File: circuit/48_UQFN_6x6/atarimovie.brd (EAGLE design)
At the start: 72.4 x 82.5 mm, 24 parts, among them IC1 AMS1117-3.3V, J1 CARTRIDGE EDGE, J2 TF-15X15, U1 DSPIC33CKXXMC105-X_M4, U2 74LVCH245APW,118, U3 74LVCH245APW,118, X1 22-23-2051

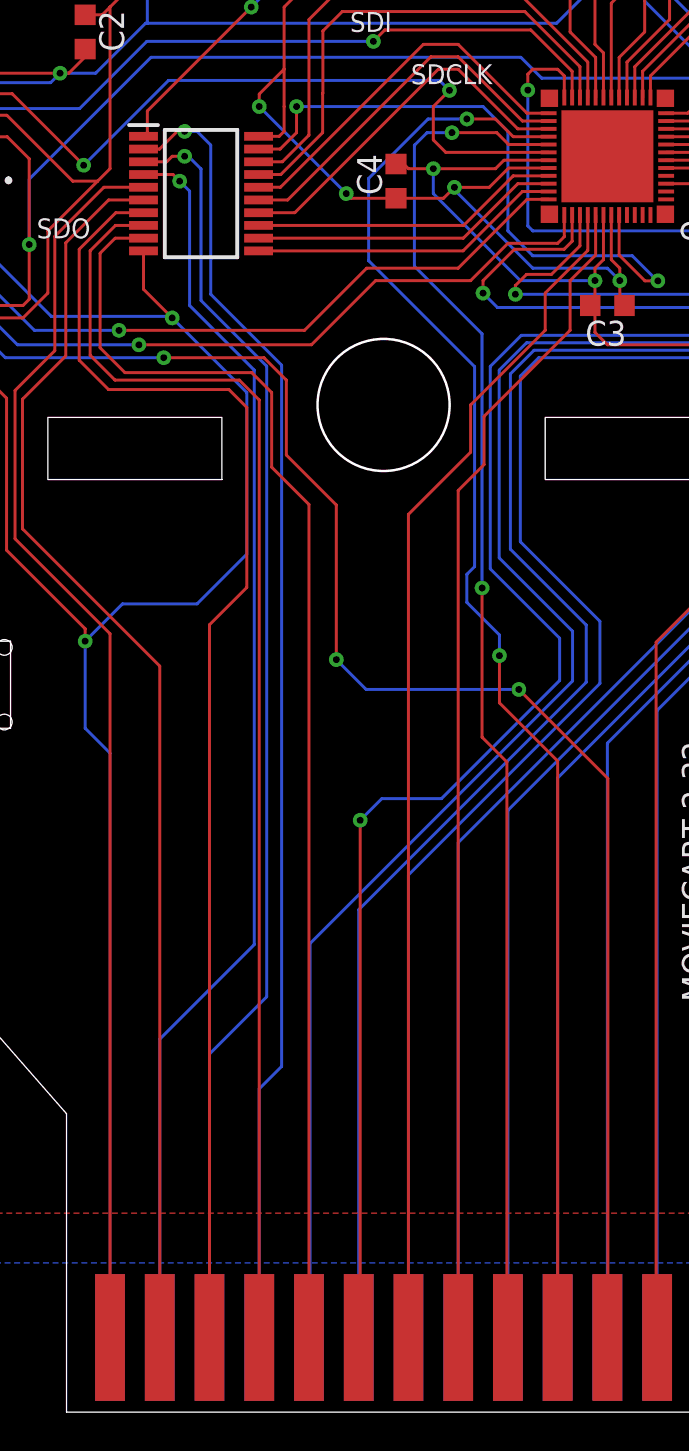
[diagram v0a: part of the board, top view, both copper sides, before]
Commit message: gerber files and rerouting away from post hole slightly
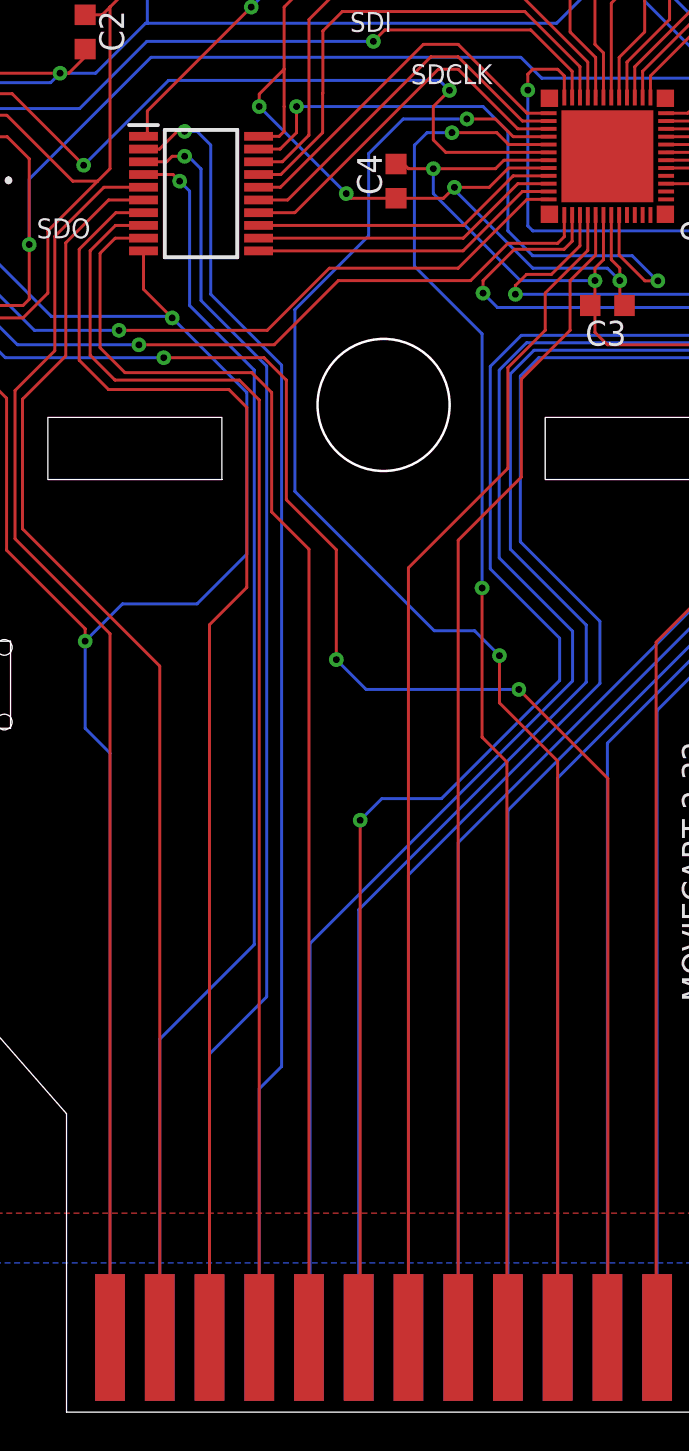
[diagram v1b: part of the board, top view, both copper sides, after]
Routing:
- net CADDR8: track 74.3 -> 79.1 mm
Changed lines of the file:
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@@
 <wire x1="42.7482" y1="38.6334" x2="42.7482" y2="36.2204" width="0.1524" layer="1"/>
 <wire x1="45.72" y1="3.81" x2="45.72" y2="33.2486" width="0.1524" layer="1"/>
-<wire x1="41.0845" y1="66.04" x2="39.1033" y2="66.04" width="0.1524" layer="16"/>
+<wire x1="41.0845" y1="66.04" x2="37.8333" y2="66.04" width="0.1524" layer="16"/>
 <via x="42.7482" y="38.6334" extent="1-16" drill="0.35"/>
-<wire x1="36.068" y1="58.801" x2="36.068" y2="63.0047" width="0.1524" layer="16"/>
-<wire x1="39.1033" y1="66.04" x2="36.068" y2="63.0047" width="0.1524" layer="16"/>
-<wire x1="41.4782" y1="53.3908" x2="41.4782" y2="43.18" width="0.1524" layer="16"/>
-<wire x1="41.4782" y1="53.3908" x2="36.068" y2="58.801" width="0.1524" layer="16"/>
-<wire x1="42.7482" y1="39.6875" x2="42.7482" y2="38.6334" width="0.1524" layer="16"/>
-<wire x1="41.4782" y1="43.18" x2="41.0845" y2="42.7863" width="0.1524" layer="16"/>
-<wire x1="41.0845" y1="42.7863" x2="41.0845" y2="41.3512" width="0.1524" layer="16"/>
-<wire x1="41.0845" y1="41.3512" x2="42.7482" y2="39.6875" width="0.1524" layer="16"/>
+<wire x1="36.068" y1="60.071" x2="36.068" y2="64.2747" width="0.1524" layer="16"/>
+<wire x1="37.8333" y1="66.04" x2="36.068" y2="64.2747" width="0.1524" layer="16"/>
+<wire x1="41.4782" y1="39.9034" x2="42.7482" y2="38.6334" width="0.1524" layer="16"/>
+<wire x1="41.4782" y1="39.9034" x2="39.41705" y2="39.9034" width="0.1524" layer="16"/>
+<wire x1="39.41705" y1="39.9034" x2="32.3013" y2="47.01915" width="0.1524" layer="16"/>
+<wire x1="32.3013" y1="56.3043" x2="36.068" y2="60.071" width="0.1524" layer="16"/>
+<wire x1="32.3013" y1="47.01915" x2="32.3013" y2="56.3043" width="0.1524" layer="16"/>
 </signal>
 <signal name="CADDR9">
@@
 <wire x1="47.26" y1="59.325" x2="45.085" y2="57.15" width="0.1524" layer="1"/>
 <wire x1="45.085" y1="57.15" x2="45.085" y2="55.245" width="0.1524" layer="1"/>
-<wire x1="38.1" y1="3.81" x2="38.1" y2="45.847" width="0.1524" layer="1"/>
-<wire x1="38.1" y1="45.847" x2="41.275" y2="49.022" width="0.1524" layer="1"/>
-<wire x1="41.275" y1="49.022" x2="41.275" y2="51.435" width="0.1524" layer="1"/>
-<wire x1="45.085" y1="55.245" x2="41.275" y2="51.435" width="0.1524" layer="1"/>
+<wire x1="38.1" y1="3.81" x2="38.1" y2="43.1165" width="0.1524" layer="1"/>
+<wire x1="38.1" y1="43.1165" x2="43.18" y2="48.1965" width="0.1524" layer="1"/>
+<wire x1="43.18" y1="48.1965" x2="43.18" y2="53.34" width="0.1524" layer="1"/>
+<wire x1="45.085" y1="55.245" x2="43.18" y2="53.34" width="0.1524" layer="1"/>
 </signal>
 <signal name="CADDR12">
@@
 <wire x1="45.259996875" y1="61.935" x2="44.155" y2="61.935" width="0.1524" layer="1"/>
 <wire x1="44.155" y1="61.935" x2="40.64" y2="58.42" width="0.1524" layer="1"/>
-<wire x1="32.7914" y1="55.245" x2="23.3172" y2="55.245" width="0.1524" layer="1"/>
-<wire x1="35.9664" y1="58.42" x2="32.7914" y2="55.245" width="0.1524" layer="1"/>
-<wire x1="40.64" y1="58.42" x2="35.9664" y2="58.42" width="0.1524" layer="1"/>
+<wire x1="30.8864" y1="55.245" x2="23.3172" y2="55.245" width="0.1524" layer="1"/>
+<wire x1="34.0614" y1="58.42" x2="30.8864" y2="55.245" width="0.1524" layer="1"/>
+<wire x1="40.64" y1="58.42" x2="34.0614" y2="58.42" width="0.1524" layer="1"/>
 <via x="23.3172" y="55.245" extent="1-16" drill="0.35"/>
 <wire x1="23.3172" y1="55.245" x2="18.9992" y2="55.245" width="0.1524" layer="16"/>
@@
 <contactref element="U1" pad="37"/>
 <wire x1="46.06" y1="60.03" x2="46.06" y2="61.134996875" width="0.1524" layer="1"/>
-<wire x1="24.3332" y1="54.5084" x2="33.147" y2="54.5084" width="0.1524" layer="1"/>
+<wire x1="24.3332" y1="54.5084" x2="31.242" y2="54.5084" width="0.1524" layer="1"/>
 <via x="24.3332" y="54.5084" extent="1-16" drill="0.35"/>
-<wire x1="36.4236" y1="57.785" x2="41.275" y2="57.785" width="0.1524" layer="1"/>
+<wire x1="34.5186" y1="57.785" x2="41.275" y2="57.785" width="0.1524" layer="1"/>
 <wire x1="45.72" y1="59.69" x2="46.06" y2="60.03" width="0.1524" layer="1"/>
-<wire x1="33.147" y1="54.5084" x2="36.4236" y2="57.785" width="0.1524" layer="1"/>
+<wire x1="31.242" y1="54.5084" x2="34.5186" y2="57.785" width="0.1524" layer="1"/>
 <wire x1="5.08" y1="78.74" x2="3.7465" y2="77.4065" width="0.1524" layer="16"/>
 <wire x1="3.7465" y1="68.8975" x2="3.7465" y2="77.4065" width="0.1524" layer="16"/>
@@
 <wire x1="47.66" y1="59.09" x2="46.355" y2="57.785" width="0.1524" layer="1"/>
 <wire x1="46.355" y1="57.785" x2="46.355" y2="55.245" width="0.1524" layer="1"/>
-<wire x1="40.64" y1="47.06694375" x2="40.64" y2="3.81" width="0.1524" layer="1"/>
-<wire x1="41.9608" y1="50.8508" x2="41.9608" y2="48.38774375" width="0.1524" layer="1"/>
-<wire x1="46.355" y1="55.245" x2="41.9608" y2="50.8508" width="0.1524" layer="1"/>
-<wire x1="41.9608" y1="48.38774375" x2="40.64" y2="47.06694375" width="0.1524" layer="1"/>
+<wire x1="40.64" y1="44.52694375" x2="40.64" y2="3.81" width="0.1524" layer="1"/>
+<wire x1="43.8658" y1="52.7558" x2="43.8658" y2="47.75274375" width="0.1524" layer="1"/>
+<wire x1="46.355" y1="55.245" x2="43.8658" y2="52.7558" width="0.1524" layer="1"/>
+<wire x1="43.8658" y1="47.75274375" x2="40.64" y2="44.52694375" width="0.1524" layer="1"/>
 </signal>
 <signal name="CDATA0">
@@
 <wire x1="23.622" y1="53.086" x2="30.099" y2="53.086" width="0.1524" layer="1"/>
 <wire x1="30.099" y1="53.086" x2="31.115" y2="52.07" width="0.1524" layer="1"/>
-<wire x1="31.115" y1="48.26" x2="33.02" y2="46.355" width="0.1524" layer="1"/>
-<wire x1="31.115" y1="52.07" x2="31.115" y2="48.26" width="0.1524" layer="1"/>
-<wire x1="33.02" y1="46.355" x2="33.02" y2="3.81" width="0.1524" layer="1"/>
+<wire x1="31.115" y1="45.974" x2="33.02" y2="44.069" width="0.1524" layer="1"/>
+<wire x1="31.115" y1="52.07" x2="31.115" y2="45.974" width="0.1524" layer="1"/>
+<wire x1="33.02" y1="44.069" x2="33.02" y2="3.81" width="0.1524" layer="1"/>
 <wire x1="24.5702" y1="59.95339375" x2="23.12339375" y2="59.95339375" width="0.1524" layer="1"/>
 <wire x1="23.12339375" y1="59.95339375" x2="22.352" y2="59.182" width="0.1524" layer="1"/>
@@
 <wire x1="25.6032" y1="53.848" x2="30.7213" y2="53.848" width="0.1524" layer="1"/>
 <wire x1="30.7213" y1="53.848" x2="31.8643" y2="52.705" width="0.1524" layer="1"/>
-<wire x1="31.8643" y1="52.705" x2="31.8643" y2="48.8791625" width="0.1524" layer="1"/>
-<wire x1="31.8643" y1="48.8791625" x2="34.417" y2="46.3264625" width="0.1524" layer="1"/>
-<wire x1="34.417" y1="46.3264625" x2="34.417" y2="38.4302" width="0.1524" layer="1"/>
+<wire x1="31.8643" y1="52.705" x2="31.8643" y2="46.5931625" width="0.1524" layer="1"/>
+<wire x1="31.8643" y1="46.5931625" x2="34.417" y2="44.0404625" width="0.1524" layer="1"/>
+<wire x1="34.417" y1="44.0404625" x2="34.417" y2="38.4302" width="0.1524" layer="1"/>
 <contactref element="IC1" pad="3"/>
 <wire x1="12.7" y1="78.74" x2="12.7" y2="76.2" width="0.1524" layer="1"/>

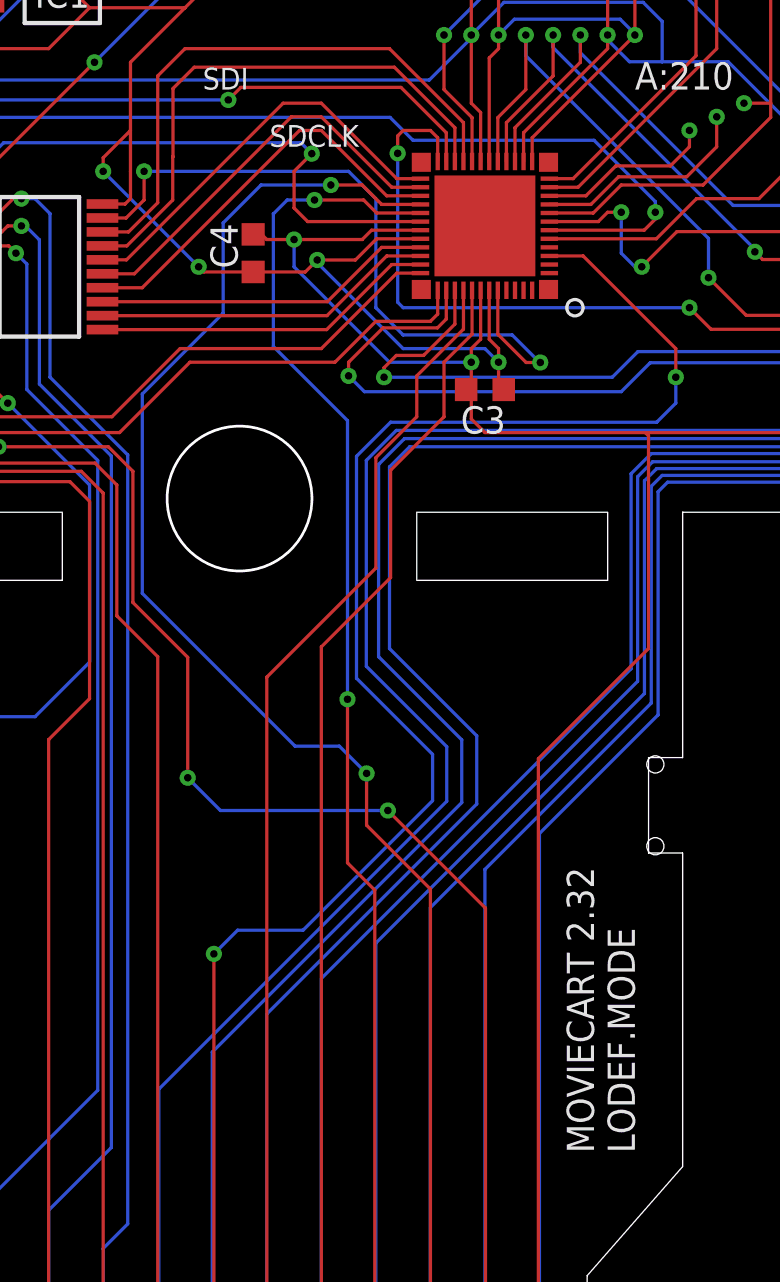
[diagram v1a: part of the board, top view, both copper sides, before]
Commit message: spaced out caddr8 caddr9 @LODEFMODE not LODEF.MODE
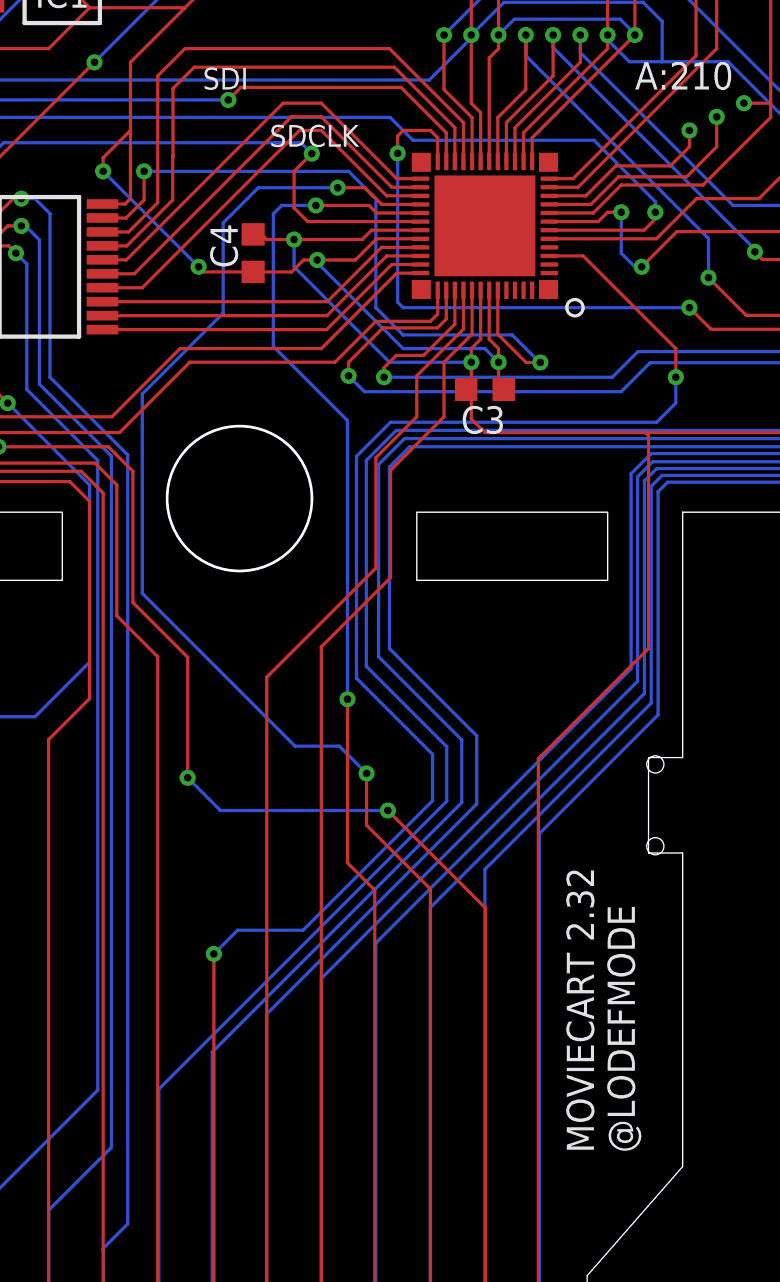
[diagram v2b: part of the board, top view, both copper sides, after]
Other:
- board text added: "@LODEFMODE"
- board text removed: "LODEF.MODE"
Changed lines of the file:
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@@
 <text x="56.0705" y="75.2475" size="1.016" layer="25">SDCS</text>
 <text x="19.1135" y="59.944" size="1.016" layer="25">SDO</text>
-<text x="55.245" y="20.955" size="1.27" layer="21" font="vector" rot="R90">LODEF.MODE</text>
+<text x="55.245" y="20.955" size="1.27" layer="21" font="vector" rot="R90">@LODEFMODE</text>
 </plain>
 <attributes>
@@
 <wire x1="55.485" y1="77.075" x2="55.485" y2="78.486" width="0.1524" layer="1"/>
 <wire x1="55.245" y1="76.835" x2="55.485" y2="77.075" width="0.1524" layer="1"/>
-<wire x1="40.4495" y1="62.5475" x2="39.892" y2="61.99" width="0.1524" layer="1"/>
+<wire x1="40.4495" y1="62.5475" x2="39.8145" y2="62.5475" width="0.1524" layer="1"/>
+<wire x1="39.8145" y1="62.5475" x2="39.257" y2="61.99" width="0.1524" layer="1"/>
 <wire x1="55.485" y1="78.486" x2="57.349909375" y2="80.01" width="0.1524" layer="1"/>
 <wire x1="57.349909375" y1="80.01" x2="69.85" y2="80.01" width="0.1524" layer="1"/>
-<wire x1="39.892" y1="61.99" x2="37.465" y2="61.99" width="0.1524" layer="1"/>
+<wire x1="39.257" y1="61.99" x2="37.465" y2="61.99" width="0.1524" layer="1"/>
 <wire x1="49.6316" y1="73.7616" x2="48.895" y2="73.025" width="0.1524" layer="16"/>
 <wire x1="54.5592" y1="73.7616" x2="49.6316" y2="73.7616" width="0.1524" layer="16"/>
@@
 <contactref element="IC1" pad="2"/>
 <contactref element="J2" pad="4"/>
-<wire x1="31.75" y1="65.405" x2="31.75" y2="66.675" width="0.1524" layer="1"/>
 <via x="34.925" y="62.23" extent="1-16" drill="0.35"/>
 <wire x1="34.925" y1="62.23" x2="35.165" y2="61.99" width="0.1524" layer="1"/>
@@
 <wire x1="38.1" y1="76.2" x2="38.95" y2="77.05" width="0.1524" layer="1"/>
 <wire x1="38.95" y1="77.05" x2="38.95" y2="77.255" width="0.1524" layer="1"/>
-<wire x1="31.75" y1="66.675" x2="31.75" y2="68.58" width="0.1524" layer="1"/>
+<wire x1="31.75" y1="65.405" x2="31.75" y2="68.58" width="0.1524" layer="1"/>
 <wire x1="31.75" y1="68.58" x2="31.75" y2="71.755" width="0.1524" layer="1"/>
 <wire x1="31.75" y1="71.755" x2="34.29" y2="74.295" width="0.1524" layer="1"/>
@@
 <contactref element="U1" pad="28"/>
 <wire x1="45.259996875" y1="65.135" x2="43.45" y2="65.135" width="0.1524" layer="1"/>
-<wire x1="43.45" y1="65.135" x2="42.545" y2="66.04" width="0.1524" layer="1"/>
-<via x="41.0845" y="66.04" extent="1-16" drill="0.35"/>
-<wire x1="42.545" y1="66.04" x2="41.0845" y2="66.04" width="0.1524" layer="1"/>
+<wire x1="43.45" y1="65.135" x2="42.672" y2="65.913" width="0.1524" layer="1"/>
+<via x="41.402" y="65.913" extent="1-16" drill="0.35"/>
+<wire x1="42.672" y1="65.913" x2="41.402" y2="65.913" width="0.1524" layer="1"/>
 <wire x1="45.72" y1="33.2486" x2="42.7482" y2="36.2204" width="0.1524" layer="1"/>
 <wire x1="42.7482" y1="38.6334" x2="42.7482" y2="36.2204" width="0.1524" layer="1"/>
 <wire x1="45.72" y1="3.81" x2="45.72" y2="33.2486" width="0.1524" layer="1"/>
-<wire x1="41.0845" y1="66.04" x2="37.8333" y2="66.04" width="0.1524" layer="16"/>
+<wire x1="41.402" y1="65.913" x2="37.7063" y2="65.913" width="0.1524" layer="16"/>
 <via x="42.7482" y="38.6334" extent="1-16" drill="0.35"/>
 <wire x1="36.068" y1="60.071" x2="36.068" y2="64.2747" width="0.1524" layer="16"/>
-<wire x1="37.8333" y1="66.04" x2="36.068" y2="64.2747" width="0.1524" layer="16"/>
+<wire x1="37.7063" y1="65.913" x2="36.068" y2="64.2747" width="0.1524" layer="16"/>
 <wire x1="41.4782" y1="39.9034" x2="42.7482" y2="38.6334" width="0.1524" layer="16"/>
 <wire x1="41.4782" y1="39.9034" x2="39.41705" y2="39.9034" width="0.1524" layer="16"/>
@@
 <contactref element="U1" pad="29"/>
 <wire x1="45.259996875" y1="64.735" x2="43.215" y2="64.735" width="0.1524" layer="1"/>
-<wire x1="43.215" y1="64.735" x2="42.6085" y2="65.3415" width="0.1524" layer="1"/>
-<via x="40.3225" y="65.3415" extent="1-16" drill="0.35"/>
-<wire x1="42.6085" y1="65.3415" x2="40.3225" y2="65.3415" width="0.1524" layer="1"/>
+<wire x1="43.215" y1="64.735" x2="42.8625" y2="65.0875" width="0.1524" layer="1"/>
+<via x="40.386" y="65.0875" extent="1-16" drill="0.35"/>
+<wire x1="42.8625" y1="65.0875" x2="40.386" y2="65.0875" width="0.1524" layer="1"/>
 <wire x1="38.4048" y1="58.5216" x2="38.4048" y2="64.7065" width="0.1524" layer="16"/>
-<wire x1="39.0525" y1="65.3415" x2="38.4175" y2="64.7065" width="0.1524" layer="16"/>
-<wire x1="39.0525" y1="65.3415" x2="40.3225" y2="65.3415" width="0.1524" layer="16"/>
+<wire x1="38.7985" y1="65.0875" x2="38.4175" y2="64.7065" width="0.1524" layer="16"/>
+<wire x1="38.7985" y1="65.0875" x2="40.386" y2="65.0875" width="0.1524" layer="16"/>
 <wire x1="38.4175" y1="64.7065" x2="38.4048" y2="64.7065" width="0.1524" layer="16"/>
 <wire x1="43.18" y1="3.81" x2="43.1292" y2="3.81" width="0.1524" layer="1"/>
